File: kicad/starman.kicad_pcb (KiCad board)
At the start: 4 copper layers, 182 x 150 mm, 206 parts, among them J1 M20-8771246, J10 Barrel_Jack_MountingPin, J2 M20-8771246, J3 M20-8771246, J4 ESW-106-44-T-S, J5 Conn_02x03_Counter_Clockwise, J6 ESW-112-44-T-S, J7 Conn_01x10, J8 ESW-112-44-T-S, J9 Conn_01x10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

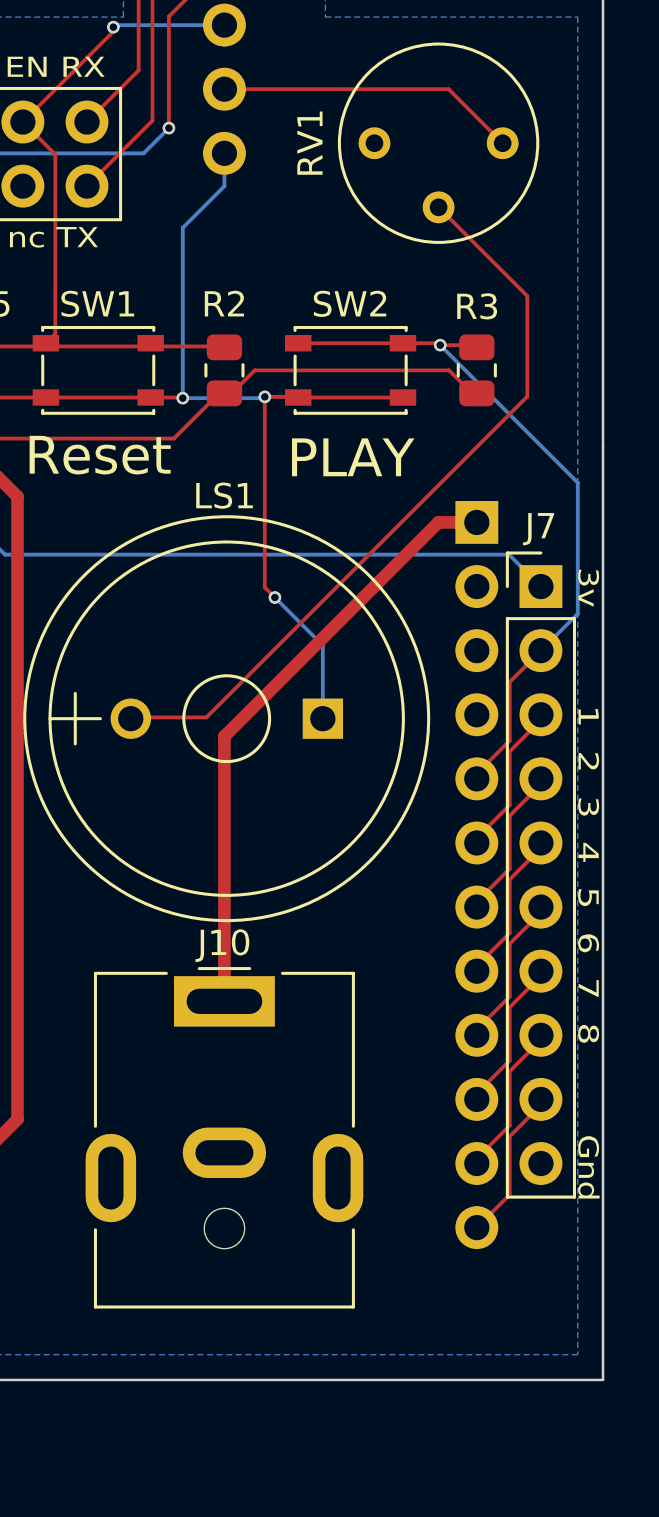
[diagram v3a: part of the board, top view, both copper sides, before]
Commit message: Add on headers for an external "Play" button
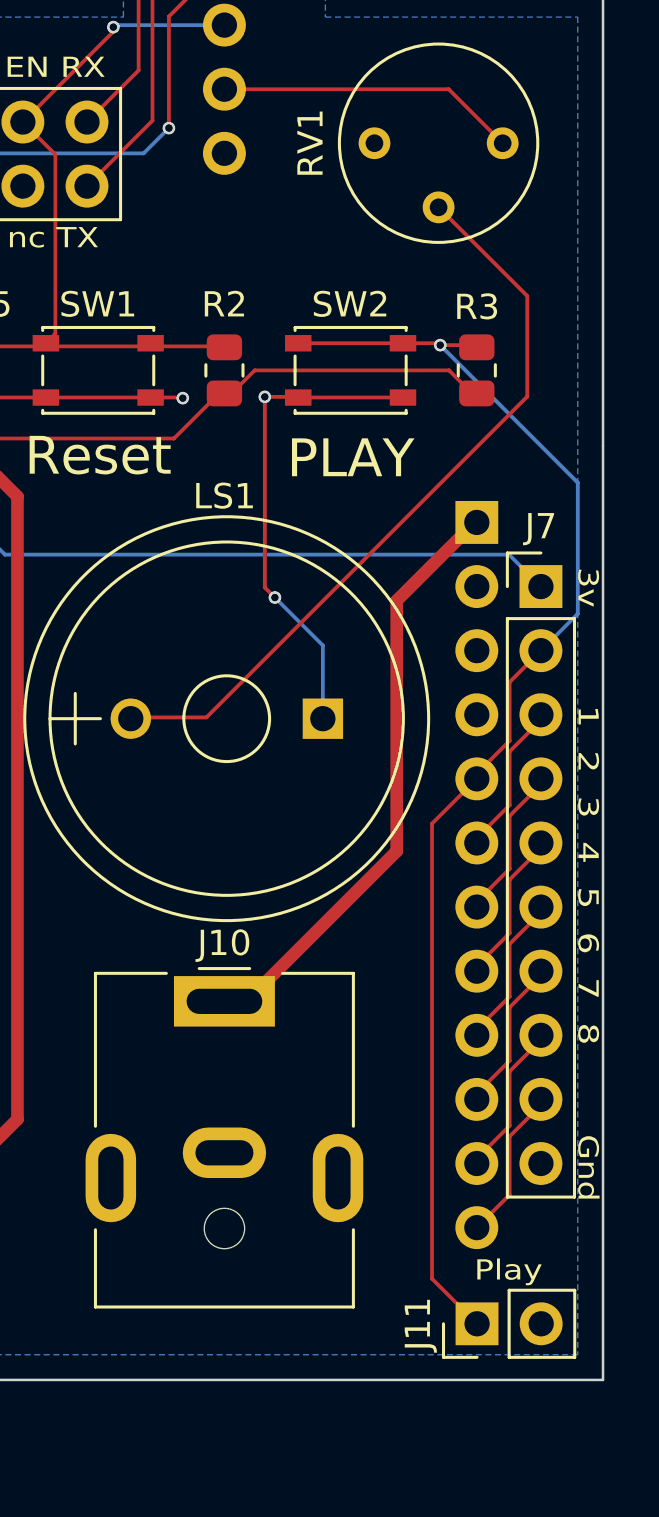
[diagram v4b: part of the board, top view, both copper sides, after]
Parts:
- added J11: Conn_02x01, Connector_PinHeader_2.54mm:PinHeader_1x02_P2.54mm_Vertical, F.Cu at (207.0, 147.8)
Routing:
- net /ext_GPIO1: track 28.2 -> 51.3 mm
- net GNDA: track 44.0 -> 30.4 mm
- net VCC: track 24.7 -> 24.0 mm
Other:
- board text added: "Play"
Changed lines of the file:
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@@
+    )
+  )
+  (footprint "Connector_PinHeader_2.54mm:PinHeader_1x02_P2.54mm_Vertical" (layer "F.Cu")
+    (at 207.01 147.775 90)
+    (descr "Through hole straight pin header, 1x02, 2.54mm pitch, single row")
+    (tags "Through hole pin header THT 1x02 2.54mm single row")
+    (property "Sheetfile" "starman.kicad_sch")
+    (property "Sheetname" "")
+    (attr through_hole)
+    (fp_text reference "J11" (at 0 -2.33 90) (layer "F.SilkS")
+      (effects (font (size 1 1) (thickness 0.15)))
+    )
+    (fp_text value "Conn_02x01" (at 0 4.87 90) (layer "F.Fab")
+      (effects (font (size 1 1) (thickness 0.15)))
+    )
+    (fp_text user "${REFERENCE}" (at 0 1.27) (layer "F.Fab")
+      (effects (font (size 1 1) (thickness 0.15)))
+    )
+    (fp_line (start -1.33 3.87) (end 1.33 3.87) (layer "F.SilkS") (width 0.12))
+    (fp_line (start -1.33 -1.33) (end 0 -1.33) (layer "F.SilkS") (width 0.12))
+    (fp_line (start 1.33 1.27) (end 1.33 3.87) (layer "F.SilkS") (width 0.12))
+    (fp_line (start -1.33 0) (end -1.33 -1.33) (layer "F.SilkS") (width 0.12))
+    (fp_line (start -1.33 1.27) (end -1.33 3.87) (layer "F.SilkS") (width 0.12))
+    (fp_line (start -1.33 1.27) (end 1.33 1.27) (layer "F.SilkS") (width 0.12))
+    (fp_line (start 1.8 4.35) (end 1.8 -1.8) (layer "F.CrtYd") (width 0.05))
+    (fp_line (start -1.8 4.35) (end 1.8 4.35) (layer "F.CrtYd") (width 0.05))
+    (fp_line (start -1.8 -1.8) (end -1.8 4.35) (layer "F.CrtYd") (width 0.05))
+    (fp_line (start 1.8 -1.8) (end -1.8 -1.8) (layer "F.CrtYd") (width 0.05))
+    (fp_line (start -0.635 -1.27) (end 1.27 -1.27) (layer "F.Fab") (width 0.1))
+    (fp_line (start -1.27 3.81) (end -1.27 -0.635) (layer "F.Fab") (width 0.1))
+    (fp_line (start 1.27 -1.27) (end 1.27 3.81) (layer "F.Fab") (width 0.1))
+    (fp_line (start 1.27 3.81) (end -1.27 3.81) (layer "F.Fab") (width 0.1))
+    (fp_line (start -1.27 -0.635) (end -0.635 -1.27) (layer "F.Fab") (width 0.1))
+    (pad "1" thru_hole rect (at 0 0 90) (size 1.7 1.7) (drill 1) (layers *.Cu *.Mask)
+      (net 223 "/ext_GPIO1") (pinfunction "Pin_1") (pintype "passive"))
+    (pad "2" thru_hole oval (at 0 2.54 90) (size 1.7 1.7) (drill 1) (layers *.Cu *.Mask)
+      (net 232 "GNDA") (pinfunction "Pin_2") (pintype "passive"))
+    (model "${KICAD6_3DMODEL_DIR}/Connector_PinHeader_2.54mm.3dshapes/PinHeader_1x02_P2.54mm_Vertical.wrl"
+      (offset (xyz 0 0 0))
+      (scale (xyz 1 1 1))
+      (rotate (xyz 0 0 0))
     )
   )
@@
   (gr_text "Gnd" (at 211.4 141.6 270) (layer "F.SilkS")
     (effects (font (size 0.8 0.95) (thickness 0.15)))
+  )
+  (gr_text "Play" (at 208.25 145.65) (layer "F.SilkS")
+    (effects (font (size 0.8 0.95) (thickness 0.2)))
   )
   (dimension (type aligned) (layer "Cmts.User")
@@
   (segment (start 157.2 140.7625) (end 158.2 141.7625) (width 0.15) (layer "F.Cu") (net 215))
   (segment (start 157.2 140) (end 157.2 140.7625) (width 0.15) (layer "F.Cu") (net 215))
-  (segment (start 205.475 116.025) (end 207 116.025) (width 0.5) (layer "F.Cu") (net 222))
-  (segment (start 197 135.735) (end 197 124.5) (width 0.5) (layer "F.Cu") (net 222))
-  (segment (start 197 124.5) (end 205.475 116.025) (width 0.5) (layer "F.Cu") (net 222))
+  (segment (start 206.925 116.025) (end 207 116.025) (width 0.5) (layer "F.Cu") (net 222))
+  (segment (start 197 135.735) (end 197.14 135.735) (width 0.5) (layer "F.Cu") (net 222))
+  (segment (start 203.825 119.125) (end 206.925 116.025) (width 0.5) (layer "F.Cu") (net 222))
+  (segment (start 203.825 129.05) (end 203.825 119.125) (width 0.5) (layer "F.Cu") (net 222))
+  (segment (start 197.14 135.735) (end 203.825 129.05) (width 0.5) (layer "F.Cu") (net 222))
   (segment (start 205.475 108.925) (end 205.55 109) (width 0.15) (layer "F.Cu") (net 223))
+  (segment (start 205.225 127.96) (end 207 126.185) (width 0.15) (layer "F.Cu") (net 223))
   (segment (start 207 109.0875) (end 206.9125 109) (width 0.15) (layer "F.Cu") (net 223))
   (segment (start 199.925 108.925) (end 204.075 108.925) (width 0.15) (layer "F.Cu") (net 223))
   (segment (start 204.075 108.925) (end 205.475 108.925) (width 0.15) (layer "F.Cu") (net 223))
   (segment (start 208.3 124.676428) (end 207 125.976428) (width 0.15) (layer "F.Cu") (net 223))
+  (segment (start 207.01 147.775) (end 205.225 145.99) (width 0.15) (layer "F.Cu") (net 223))
   (segment (start 209.54 121.11) (end 208.3 122.35) (width 0.15) (layer "F.Cu") (net 223))
   (segment (start 209.54 121.105) (end 209.54 121.11) (width 0.15) (layer "F.Cu") (net 223))
+  (segment (start 205.225 145.99) (end 205.225 127.96) (width 0.15) (layer "F.Cu") (net 223))
   (segment (start 208.3 122.35) (end 208.3 124.676428) (width 0.15) (layer "F.Cu") (net 223))
   (segment (start 207 125.976428) (end 207 126.185) (width 0.15) (layer "F.Cu") (net 223))
@@
   (via (at 195.35 111.1) (size 0.5) (drill 0.3) (layers "F.Cu" "B.Cu") (net 232))
   (segment (start 200.9 120.9) (end 200.9 123.8) (width 0.15) (layer "B.Cu") (net 232))
-  (segment (start 197 102.7) (end 197 101.4) (width 0.15) (layer "B.Cu") (net 232))
-  (segment (start 195.35 111.1) (end 195.35 104.35) (width 0.15) (layer "B.Cu") (net 232))
   (segment (start 199 119) (end 200.9 120.9) (width 0.15) (layer "B.Cu") (net 232))
-  (segment (start 195.35 111.1) (end 198.55 111.1) (width 0.15) (layer "B.Cu") (net 232))
-  (segment (start 198.55 111.1) (end 198.6 111.05) (width 0.15) (layer "B.Cu") (net 232))
-  (segment (start 195.35 104.35) (end 197 102.7) (width 0.15) (layer "B.Cu") (net 232))
   (segment (start 187.04 121.115) (end 184.5 121.115) (width 0.15) (layer "F.Cu") (net 233))
   (segment (start 187.04 123.655) (end 184.5 123.655) (width 0.15) (layer "F.Cu") (net 234))
